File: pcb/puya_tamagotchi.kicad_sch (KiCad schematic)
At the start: 0 parts

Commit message: Add PUYA PY32F002B
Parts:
- added C1, C2: 100nF, PCM_JLCPCB:C_0402, symbol PCM_JLCPCB-Capacitors:0402,100nF
- added C3: 4.7uF, PCM_JLCPCB:C_0603, symbol PCM_JLCPCB-Capacitors:0603,4.7uF
- added J1: FLASHING ONLY, Connector_PinSocket_2.54mm:PinSocket_1x04_P2.54mm_Vertical, symbol Connector:Conn_01x04_Socket
- added TP1, TP2: TestPoint, TestPoint:TestPoint_Pad_D1.0mm, symbol Connector:TestPoint
- added U1: PY32F002BF15U6TR, Tamagotchi_footprints:QFN-20_L3.0-W3.0-P0.40-TL-EP1.7, symbol Tamagotchi_parts:PY32F002BF15U6TR
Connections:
- new net: C1.2, U1.1 (PC0-NRST)
- new net +3V8: C2.2, C3.2, J1.4 (Pin_4), TP2.1, U1.6 (VCC)
- new net GND: C1.1, C2.1, C3.1, J1.1 (Pin_1), TP1.1, U1.21 (EP), U1.4 (VSS)
- new net SWCLK: J1.3 (Pin_3), U1.15 (PA2-SWC)
- new net SWDIO: J1.2 (Pin_2), U1.5 (PB6-SWD)

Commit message: Add Peripherals
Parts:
- added R1: GL5528, OptoDevice:R_LDR_5.1x4.3mm_P3.4mm_Vertical, symbol Device:R_Photo
- added R2: 20kΩ, PCM_JLCPCB:R_0402, symbol PCM_JLCPCB-Resistors:0402,20kΩ
- added R3, R4: 4.7kΩ, PCM_JLCPCB:R_0402, symbol PCM_JLCPCB-Resistors:0402,4.7kΩ
- added SW1, SW2, SW3, SW4: TS-1187A-B-A-B, Tamagotchi_footprints:SW-SMD_4P-L5.1-W5.1-P3.70-LS6.5-TL_H1.5, symbol Tamagotchi_parts:TS-1187A-B-A-B
- added U2: OLED_128x64_SSD1306, Tamagotchi_footprints:SSD1306_OLED, symbol Tamagotchi_parts:SSD1306_OLED
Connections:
- net +3V8: now also R1.1, R3.2, R4.2, U2.2 (VCC)
- net GND: now also R2.1, SW1.3 (C), SW2.3 (C), SW3.3 (C), SW4.3 (C), U2.1 (GND)
- net at U1.12 (PB0): now also R1.2, R2.2
- net BUTTON_1: now reaches U1.17 (PA4)
- net BUTTON_1: now also SW1.1 (A)
- net BUTTON_2: now reaches U1.18 (PA5)
- net BUTTON_2: now also SW2.1 (A)
- net BUTTON_3: now reaches U1.19 (PA6)
- net BUTTON_3: now also SW3.1 (A)
- net BUTTON_4: now reaches U1.20 (PA7)
- net BUTTON_4: now also SW4.1 (A)
- net I2C.SDA: now reaches U1.8 (PB4)
- net I2C.SDA: now also R4.1, U2.4 (SDA)
- net I2C.SCL: now reaches U1.9 (PB3)
- net I2C.SCL: now also R3.1, U2.3 (SCL)
- no-connect marks 0 -> 8
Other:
- moved on the sheet: C1, C2, C3, J1, U1

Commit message: Add TPs and LEDs
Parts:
- added BZ1: Buzzer, Buzzer_Beeper:Buzzer_12x9.5RM7.6, symbol Device:Buzzer
- added D1, D2: Red, PCM_JLCPCB:D_0603, symbol PCM_JLCPCB-Diodes:LED,0603,Red
- added D3: White, PCM_JLCPCB:D_0603, symbol PCM_JLCPCB-Diodes:LED,0603,White
- added J2: ADDITIONAL, Connector_PinSocket_2.54mm:PinSocket_1x04_P2.54mm_Vertical, symbol Connector:Conn_01x04_Socket
- added Q1: 2N7002, PCM_JLCPCB:Q_SOT-23, symbol PCM_JLCPCB-Transistors:NMOS,2N7002
- added R5, R6, R7: 1kΩ, PCM_JLCPCB:R_0402, symbol PCM_JLCPCB-Resistors:0402,1kΩ
- added TP3, TP4, TP5: TestPoint, TestPoint:TestPoint_Pad_D1.0mm, symbol Connector:TestPoint
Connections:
- net +3V8: now also J2.4 (Pin_4)
- net GND: now also D2.1, D3.1, J2.1 (Pin_1)
- net LDR_OUT: now reaches R1.2, R2.2
- net LDR_OUT: now also U1.11 (PB1); no longer U1.12 (PB0)
- net at U1.13 (PA0): now also R5.1
- net at U1.14 (PA1): now also R6.1
- net PC1: now reaches U1.2 (PC1)
- net PC1: now also J2.2 (Pin_2)
- net PB7: now reaches U1.3 (PB7)
- net PB7: now also J2.3 (Pin_3)
- new net: D2.2, R5.2
- new net: D3.2, R6.2
- new net: D1.2, R7.2
- new net BUZZER: U1.12 (PB0)
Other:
- moved on the sheet: J1, R1, R2

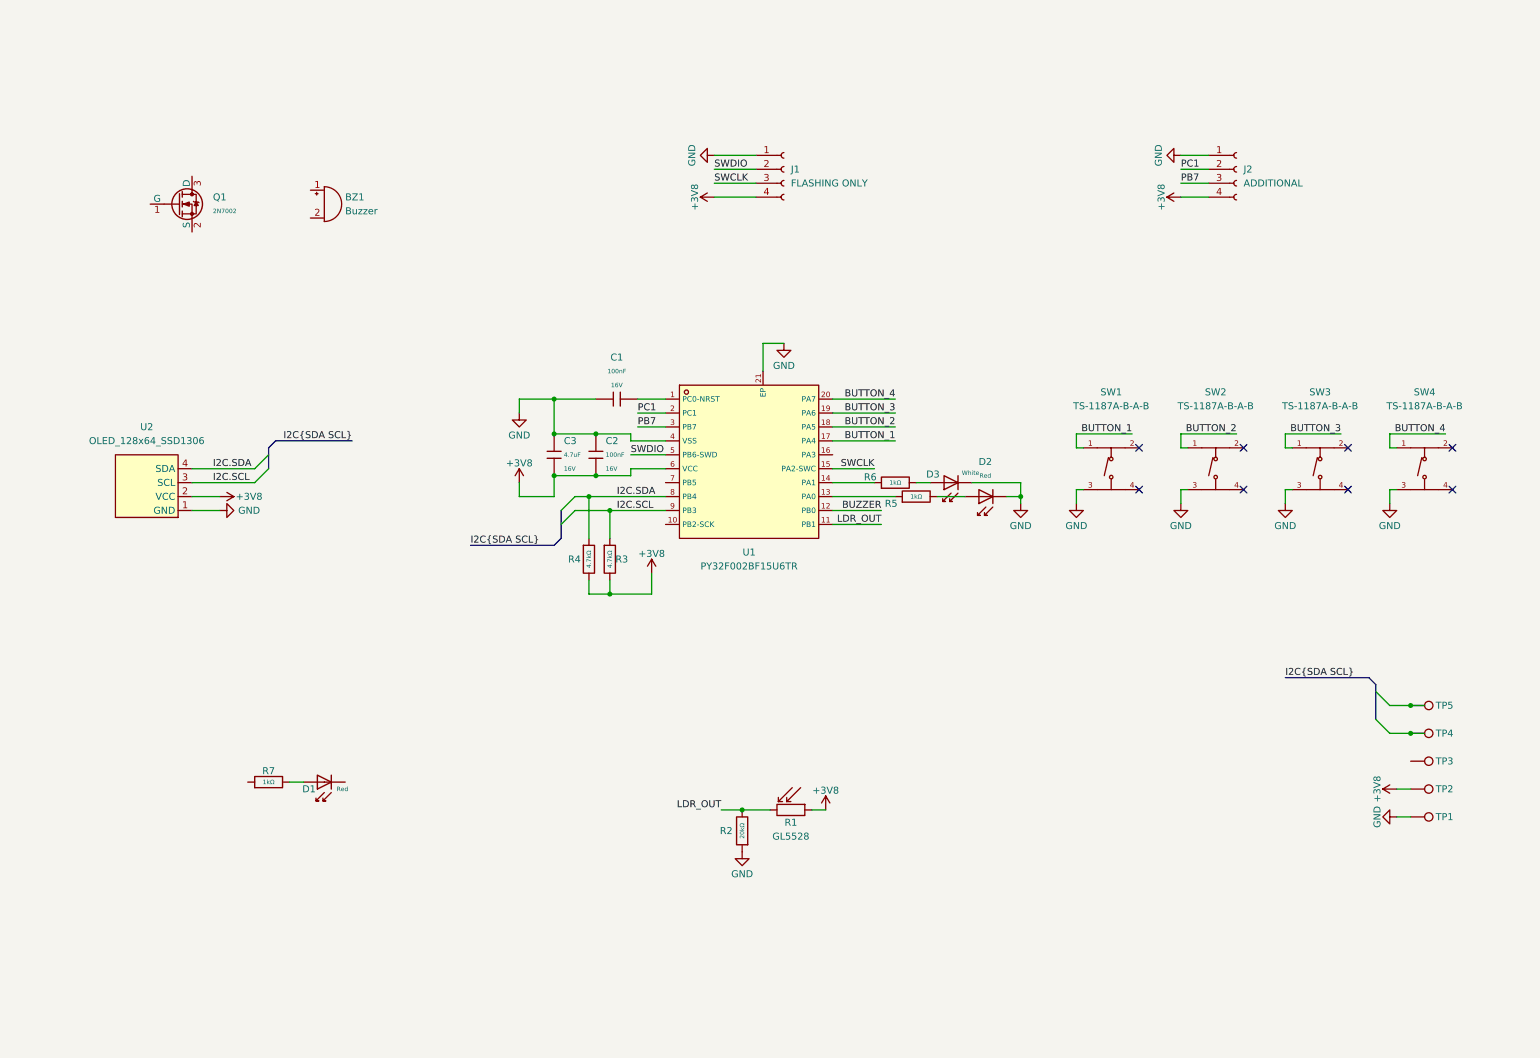
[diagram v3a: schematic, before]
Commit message: Add Buzzer
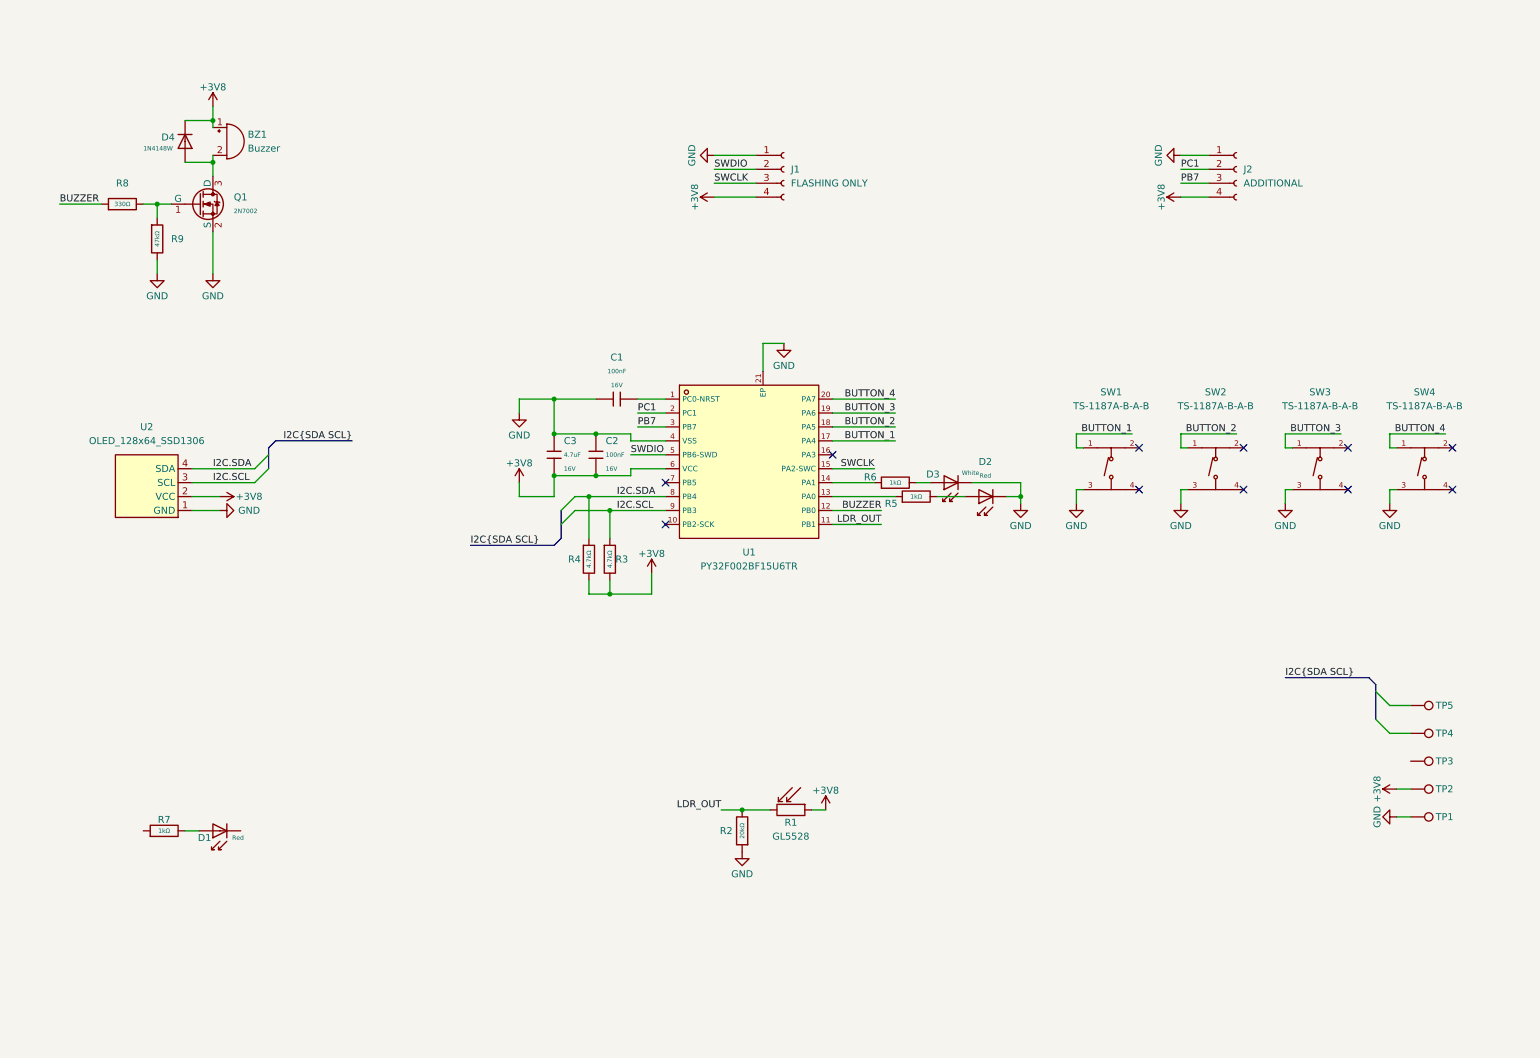
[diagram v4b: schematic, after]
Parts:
- added D4: 1N4148W, PCM_JLCPCB:D_SOD-123, symbol PCM_JLCPCB-Diodes:Switching,1N4148W
- added R8: 330Ω, PCM_JLCPCB:R_0402, symbol PCM_JLCPCB-Resistors:0402,330Ω
- added R9: 47kΩ, PCM_JLCPCB:R_0402, symbol PCM_JLCPCB-Resistors:0402,47kΩ
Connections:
- net +3V8: now also BZ1.1 (+), D4.1
- net BUZZER: now also R8.1
- net GND: now also Q1.2 (S), R9.2
- net at BZ1.2 (-): now also Q1.3 (D), D4.2
- net at Q1.1 (G): now also R8.2, R9.1
- no-connect marks 8 -> 11
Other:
- moved on the sheet: BZ1, D1, Q1, R7

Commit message: Add charging and protection, clean schematic
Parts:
- removed Q1: 2N7002, PCM_JLCPCB:Q_SOT-23, symbol PCM_JLCPCB-Transistors:NMOS,2N7002
- added C4, C5: 10uF, PCM_JLCPCB:C_0603, symbol PCM_JLCPCB-Capacitors:0603,10uF,(2)
- added C6: 100nF, PCM_JLCPCB:C_0402, symbol PCM_JLCPCB-Capacitors:0402,100nF
- added J3: BATTERY, Connector_JST:JST_EH_B2B-EH-A_1x02_P2.50mm_Vertical, symbol Connector:Conn_01x02_Socket
- added J4: USB_C_Receptacle_PowerOnly_6P, Connector_USB:USB_C_Receptacle_HRO_TYPE-C-31-M-17, symbol Connector:USB_C_Receptacle_PowerOnly_6P
- added Q1, Q2, Q3: AO3400A, PCM_JLCPCB:Q_SOT-23, symbol PCM_JLCPCB-Transistors:NMOS,AO3400A
- added R10, R11: 5.1kΩ, PCM_JLCPCB:R_0402, symbol PCM_JLCPCB-Resistors:0402,5.1kΩ
- added R12: 10kΩ, PCM_JLCPCB:R_0402, symbol PCM_JLCPCB-Resistors:0402,10kΩ
- added R13: 100Ω, PCM_JLCPCB:R_0402, symbol PCM_JLCPCB-Resistors:0402,100Ω
- added R14: 1kΩ, PCM_JLCPCB:R_0402, symbol PCM_JLCPCB-Resistors:0402,1kΩ
- added U3: TP4056, PCM_JLCPCB:ESOP-8_L4.9-W3.9-P1.27-LS6.0-BL-EP, symbol PCM_JLCPCB-Power:Battery, Li-Ion, 1.0A, TP4056
- added U4: DW01A, Package_TO_SOT_SMD:SOT-23-6, symbol Battery_Management:DW01A
- J1: value FLASHING ONLY -> SWD pins
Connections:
- net GND: now also C4.1, C5.1, J4.A12 (GND), J4.B12 (GND), J4.SH (SHIELD), Q1.2 (S), Q3.2 (S), R10.2, R11.2, R12.2, R14.2, U3.1 (TEMP), U3.3 (GND), U3.6 (STDBY#), U3.9 (EP)
- net I2C.SCL: now also TP4.1
- net I2C.SDA: now also TP5.1
- net at R8.2, R9.1: now also Q1.1 (G)
- net VBUS: now reaches R7.1
- net VBUS: now also TP3.1, C4.2, J4.A9 (VBUS), J4.B9 (VBUS), U3.4 (VCC), U3.8 (CE)
- net at BZ1.2 (-), D4.2: now also Q1.3 (D)
- net at D1.1: now also U3.7 (CHRG#)
- net +3V8 renamed +BATT
- net +BATT: now also C5.2, J3.1 (Pin_1), R13.1, U3.5 (BAT)
- new net: J4.B5 (CC2), R10.1
- new net: C6.1, R13.2, U4.5 (VCC)
- new net: Q2.1 (G), U4.1 (OD)
- new net: Q2.3 (D), Q3.3 (D)
- new net: Q3.1 (G), U4.3 (OC)
- new net: J4.A5 (CC1), R11.1
- new net: R12.1, U3.2 (PROG)
- new net: R14.1, U4.2 (CS)
- new net -BATT: C6.2, J3.2 (Pin_2), Q2.2 (S), U4.6 (GND)
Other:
- note added: "BUTTONS and LDR"
- note added: "BUZZER"
- note added: "Charging and protection"
- note added: "FLASHING"
- note added: "I2C SSD1306 OLED"
- note added: "PY32F002B QFN"
- note added: "TP and GPIO"
- moved on the sheet: BZ1, C1, C2, C3, D1, D2, D3, D4, J1, J2, R1, R2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

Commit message: Clean schematic, add load sharing
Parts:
- removed R2: 20kΩ, PCM_JLCPCB:R_0402, symbol PCM_JLCPCB-Resistors:0402,20kΩ
- added D5: SS14, PCM_JLCPCB:D_SMA, symbol PCM_JLCPCB-Diodes:Schottky,SS14
- added Q4: AO3401A, PCM_JLCPCB:Q_SOT-23, symbol PCM_JLCPCB-Transistors:PMOS,AO3401A
- added R15: 100kΩ, PCM_JLCPCB:R_0402, symbol PCM_JLCPCB-Resistors:0402,100kΩ
- added R2: 10kΩ, PCM_JLCPCB:R_0402, symbol PCM_JLCPCB-Resistors:0402,10kΩ
- added TP4: TestPoint, TestPoint:TestPoint_Pad_D1.0mm, symbol Connector:TestPoint
- renumbered TP4 to TP5, TP5 to TP6
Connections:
- net +BATT: now also Q4.3 (D), TP4.1; no longer BZ1.1 (+), C2.2, C3.2, D4.1, J1.4 (Pin_4), J2.4 (Pin_4), R1.1, R3.2, R4.2, TP2.1, U1.6 (VCC), U2.2 (VCC)
- net GND: now also R15.1, R2.2
- net LDR_OUT: now also R2.1
- net VBUS: now also D5.2, Q4.1 (G), R15.2
- net LDR_DRIVE: now reaches U1.16 (PA3)
- net LDR_DRIVE: now also R1.1
- new net VCC: BZ1.1 (+), C2.2, C3.2, D4.1, D5.1, J1.4 (Pin_4), J2.4 (Pin_4), Q4.2 (S), R3.2, R4.2, TP2.1, U1.6 (VCC), U2.2 (VCC)
- no-connect marks 11 -> 10
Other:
- note added: "R12 = 10kΩ results in 130mA charging"
- moved on the sheet: C6, J3, Q2, Q3, R13, R14, TP2, TP3, U4

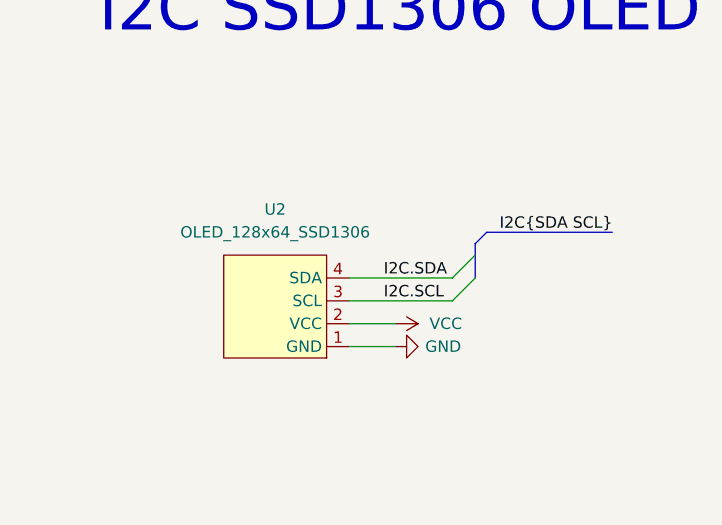
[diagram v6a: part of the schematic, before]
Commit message: Add SSH1107 OLED to schematic
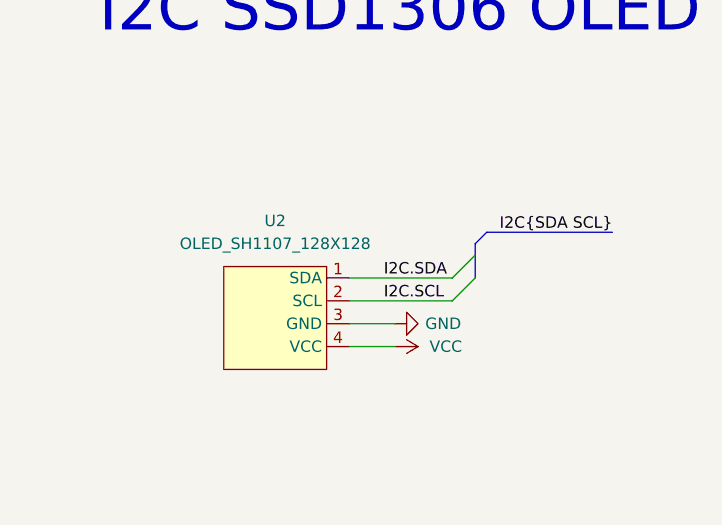
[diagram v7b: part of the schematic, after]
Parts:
- removed U2: OLED_128x64_SSD1306, Tamagotchi_footprints:SSD1306_OLED, symbol Tamagotchi_parts:SSD1306_OLED
- added U2: OLED_SH1107_128X128, Tamagotchi_footprints:SH1107_128x128_OLED, symbol Tamagotchi_parts:SH1107_128x128_OLED
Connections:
- net GND: now also U2.3 (GND)
- net I2C.SCL: now also U2.2 (SCL)
- net I2C.SDA: now also U2.1 (SDA)
- net VCC: now also U2.4 (VCC)
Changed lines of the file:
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@@
 	(wire
 		(pts
-			(xy 52.07 179.07) (xy 46.99 179.07)
+			(xy 52.07 181.61) (xy 46.99 181.61)
 		)
 		(stroke
@@
 	(wire
 		(pts
-			(xy 52.07 181.61) (xy 46.99 181.61)
+			(xy 52.07 179.07) (xy 46.99 179.07)
 		)
 		(stroke
@@
 	)
 	(symbol
+		(lib_id "Tamagotchi_parts:SH1107_128x128_OLED")
+		(at 46.99 173.99 0)
+		(mirror y)
+		(unit 1)
+		(body_style 1)
+		(exclude_from_sim no)
+		(in_bom yes)
+		(on_board yes)
+		(in_pos_files yes)
+		(dnp no)
+		(fields_autoplaced yes)
+		(property "Reference" "U2"
+			(at 38.735 167.64 0)
+			(show_name no)
+			(do_not_autoplace no)
+			(effects
+				(font
+					(size 1.27 1.27)
+				)
+			)
+		)
+		(property "Value" "OLED_SH1107_128X128"
+			(at 38.735 170.18 0)
+			(show_name no)
+			(do_not_autoplace no)
+			(effects
+				(font
+					(size 1.27 1.27)
+				)
+			)
+		)
+		(property "Footprint" "Tamagotchi_footprints:SH1107_128x128_OLED"
+			(at 30.988 179.832 0)
+			(hide yes)
+			(show_name no)
+			(do_not_autoplace no)
+			(effects
+				(font
+					(size 1.27 1.27)
+				)
+				(justify left bottom)
+			)
+		)
+		(property "Datasheet" ""
+			(at 46.99 173.99 0)
+			(hide yes)
+			(show_name no)
+			(do_not_autoplace no)
+			(effects
+				(font
+					(size 1.27 1.27)
+				)
+			)
+		)
+		(property "Description" ""
+			(at 46.99 173.99 0)
+			(hide yes)
+			(show_name no)
+			(do_not_autoplace no)
+			(effects
+				(font
+					(size 1.27 1.27)
+				)
+			)
+		)
+		(pin "4"
+		)
+		(pin "2"
+		)
+		(pin "1"
+		)
+		(pin "3"
+		)
+		(instances
+			(project "puya_tamagotchi"
+				(path "/14e76ab0-d438-4b0a-9510-82497b49bc08"
+					(reference "U2")
+					(unit 1)
+				)
+			)
+		)
+	)
+	(symbol
 		(lib_id "PCM_JLCPCB-Capacitors:0603,4.7uF")
 		(at 106.68 99.06 0)
@@
 	(symbol
 		(lib_id "power:GND")
-		(at 52.07 181.61 90)
+		(at 52.07 179.07 90)
 		(unit 1)
 		(body_style 1)
@@
 		(dnp no)
 		(property "Reference" "#PWR010"
-			(at 58.42 181.61 0)
+			(at 58.42 179.07 0)
 			(hide yes)
 			(show_name no)
@@
 		)
 		(property "Value" "GND"
-			(at 57.404 181.61 90)
+			(at 57.404 179.07 90)
 			(show_name no)
 			(do_not_autoplace no)
@@
 		)
 		(property "Footprint" ""
-			(at 52.07 181.61 0)
+			(at 52.07 179.07 0)
 			(hide yes)
 			(show_name no)
@@
 		)
 		(property "Datasheet" ""
-			(at 52.07 181.61 0)
+			(at 52.07 179.07 0)
 			(hide yes)
 			(show_name no)
@@
 		)
 		(property "Description" "Power symbol creates a global label with name \"GND\" , ground"
-			(at 52.07 181.61 0)
+			(at 52.07 179.07 0)
 			(hide yes)
 			(show_name no)
@@
 	(symbol
 		(lib_id "power:VCC")
-		(at 52.07 179.07 270)
+		(at 52.07 181.61 270)
 		(unit 1)
 		(body_style 1)
@@
 		(fields_autoplaced yes)
 		(property "Reference" "#PWR044"
-			(at 48.26 179.07 0)
+			(at 48.26 181.61 0)
 			(hide yes)
 			(show_name no)
@@
 		)
 		(property "Value" "VCC"
-			(at 55.88 179.0699 90)
+			(at 55.88 181.6099 90)
 			(show_name no)
 			(do_not_autoplace no)
@@
 		)
 		(property "Footprint" ""
-			(at 52.07 179.07 0)
+			(at 52.07 181.61 0)
 			(hide yes)
 			(show_name no)
@@
 		)
 		(property "Datasheet" ""
-			(at 52.07 179.07 0)
+			(at 52.07 181.61 0)
 			(hide yes)
 			(show_name no)
@@
 		)
 		(property "Description" "Power symbol creates a global label with name \"VCC\""
-			(at 52.07 179.07 0)
+			(at 52.07 181.61 0)
 			(hide yes)
 			(show_name no)
@@
 					(unit 1)
 				)
-			)
-		)
-	)
-	(symbol
-		(lib_id "Tamagotchi_parts:SSD1306_OLED")
-		(at 46.99 181.61 180)
-		(unit 1)
-		(body_style 1)
-		(exclude_from_sim no)
-		(in_bom yes)
-		(on_board yes)
-		(in_pos_files yes)
-		(dnp no)
-		(fields_autoplaced yes)
-		(property "Reference" "U2"
-			(at 38.735 166.37 0)
-			(show_name no)
-			(do_not_autoplace no)
-			(effects
-				(font
-					(size 1.27 1.27)
-				)
-			)
-		)
-		(property "Value" "OLED_128x64_SSD1306"
-			(at 38.735 168.91 0)
-			(show_name no)
-			(do_not_autoplace no)
-			(effects
-				(font
-					(size 1.27 1.27)
-				)
-			)
-		)
-		(property "Footprint" "Tamagotchi_footprints:SSD1306_OLED"
-			(at 30.988 175.768 0)
-			(hide yes)
-			(show_name no)
-			(do_not_autoplace no)
-			(effects
-				(font
-					(size 1.27 1.27)
-				)
-				(justify left bottom)
-			)
-		)
-		(property "Datasheet" ""
-			(at 46.99 181.61 0)
-			(hide yes)
-			(show_name no)
-			(do_not_autoplace no)
-			(effects
-				(font
-					(size 1.27 1.27)
-				)
-			)
-		)
-		(property "Description" ""
-			(at 46.99 181.61 0)
-			(hide yes)
-			(show_name no)
-			(do_not_autoplace no)
-			(effects
-				(font
-					(size 1.27 1.27)
-				)
-			)
-		)
-		(pin "1"
-		)
-		(pin "4"
-		)
-		(pin "3"
-		)
-		(pin "2"
-		)
-		(instances
-			(project "puya_tamagotchi"
-				(path "/14e76ab0-d438-4b0a-9510-82497b49bc08"
-					(reference "U2")
-					(unit 1)
-				)
